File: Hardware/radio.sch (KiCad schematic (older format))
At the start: 8 parts

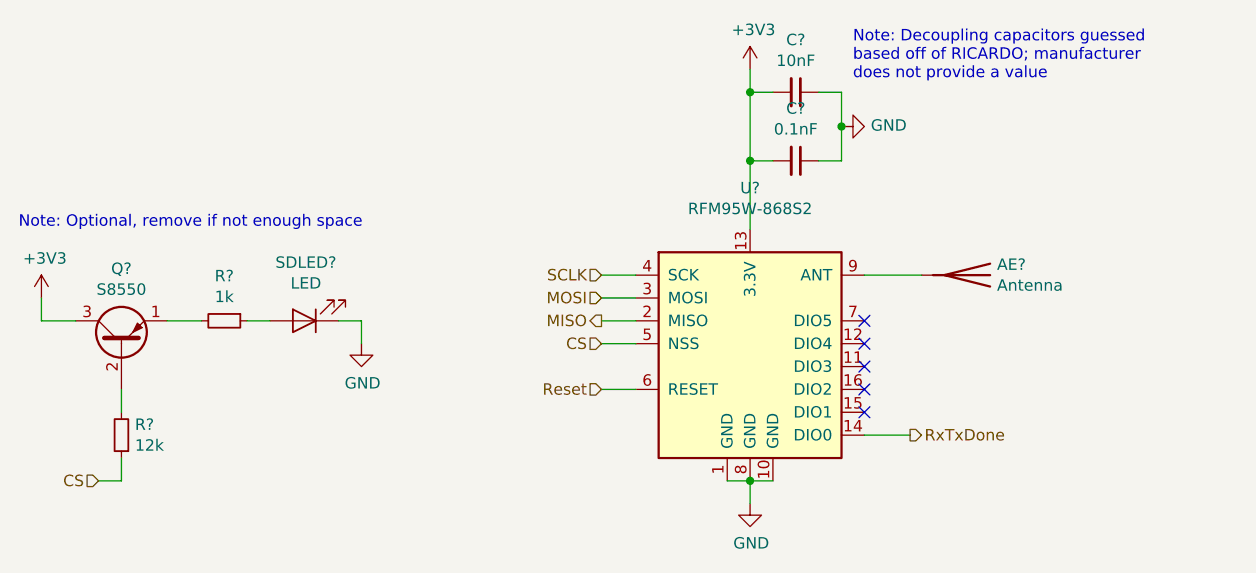
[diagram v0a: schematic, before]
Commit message: Fixed some of the ERC errors
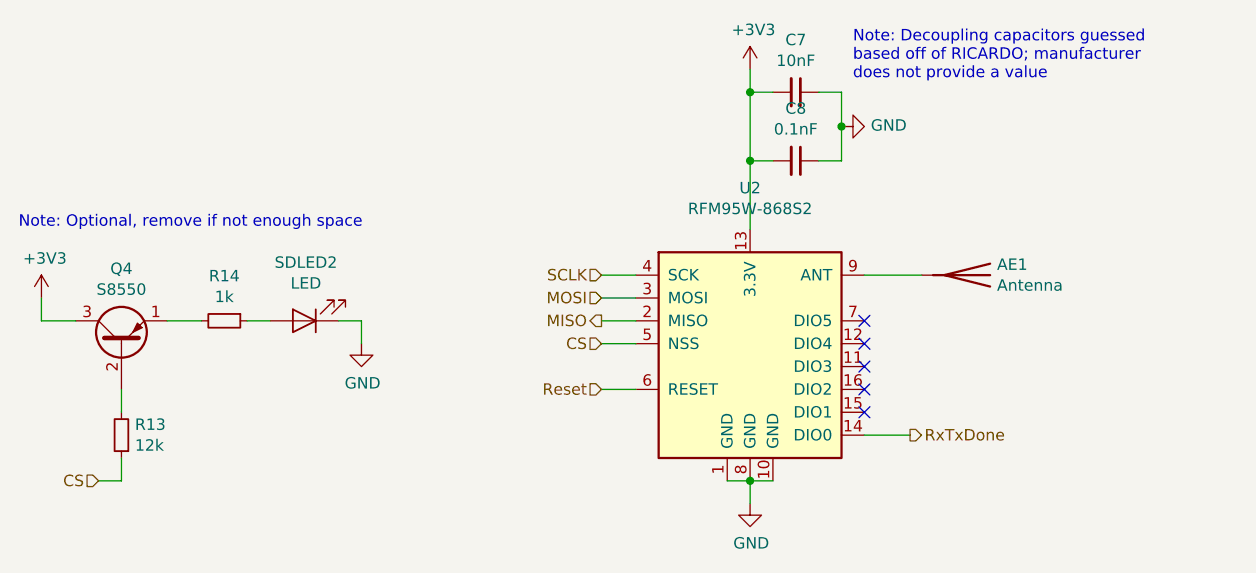
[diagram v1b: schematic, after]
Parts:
- gave numbers to parts that had none: 8
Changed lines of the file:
@@
 $EndDescr
 $Comp
-L RF_Module:RFM95W-868S2 U?
+L RF_Module:RFM95W-868S2 U2
 U 1 1 606C3788
 P 6550 3750
-F 0 "U?" H 6550 4431 50  0000 C CNN
+F 0 "U2" H 6550 4431 50  0000 C CNN
 F 1 "RFM95W-868S2" H 6550 4340 50  0000 C CNN
 F 2 "" H 3250 5400 50  0001 C CNN
@@
 	6550 4350 6550 4450
 $Comp
-L power:GND #PWR0106
+L power:GND #PWR024
 U 1 1 606C4DD1
 P 6550 4450
-F 0 "#PWR0106" H 6550 4200 50  0001 C CNN
+F 0 "#PWR024" H 6550 4200 50  0001 C CNN
 F 1 "GND" H 6555 4277 50  0000 C CNN
 F 2 "" H 6550 4450 50  0001 C CNN
@@
 Connection ~ 6550 2950
 $Comp
-L Device:C_Small C?
+L Device:C_Small C8
 U 1 1 606D342D
 P 6750 2950
-F 0 "C?" V 6521 2950 50  0000 C CNN
+F 0 "C8" V 6521 2950 50  0000 C CNN
 F 1 "0.1nF" V 6612 2950 50  0000 C CNN
 F 2 "" H 6750 2950 50  0001 C CNN
@@
 $EndComp
 $Comp
-L power:+3V3 #PWR0108
+L power:+3V3 #PWR023
 U 1 1 606D3D70
 P 6550 2550
-F 0 "#PWR0108" H 6550 2400 50  0001 C CNN
+F 0 "#PWR023" H 6550 2400 50  0001 C CNN
 F 1 "+3V3" H 6565 2723 50  0000 C CNN
 F 2 "" H 6550 2550 50  0001 C CNN
@@
 	6550 2650 6550 2950
 $Comp
-L Device:C_Small C?
+L Device:C_Small C7
 U 1 1 606DCDA4
 P 6750 2650
-F 0 "C?" V 6521 2650 50  0000 C CNN
+F 0 "C7" V 6521 2650 50  0000 C CNN
 F 1 "10nF" V 6612 2650 50  0000 C CNN
 F 2 "" H 6750 2650 50  0001 C CNN
@@
 $EndComp
 $Comp
-L power:GND #PWR0109
+L power:GND #PWR025
 U 1 1 606DD712
 P 6950 2800
-F 0 "#PWR0109" H 6950 2550 50  0001 C CNN
+F 0 "#PWR025" H 6950 2550 50  0001 C CNN
 F 1 "GND" V 6955 2672 50  0000 R CNN
 F 2 "" H 6950 2800 50  0001 C CNN
@@
 	7050 3450 7300 3450
 $Comp
-L Device:Antenna AE?
+L Device:Antenna AE1
 U 1 1 606E40D7
 P 7500 3450
-F 0 "AE?" V 7454 3580 50  0000 L CNN
+F 0 "AE1" V 7454 3580 50  0000 L CNN
 F 1 "Antenna" V 7545 3580 50  0000 L CNN
 F 2 "" H 7500 3450 50  0001 C CNN
@@
 P 4600 3650
 AR Path="/6068D50F/60A90342" Ref="SDLED?"  Part="1"
-AR Path="/606B714B/60A90342" Ref="RadioLED?"  Part="1"
-F 0 "RadioLED?" H 4593 3395 50  0000 C CNN
+AR Path="/606B714B/60A90342" Ref="SDLED2"  Part="1"
+F 0 "SDLED2" H 4593 3395 50  0000 C CNN
 F 1 "LED" H 4593 3486 50  0000 C CNN
 F 2 "" H 4600 3650 50  0001 C CNN
@@
 	3450 3650 3450 3550
 $Comp
-L power:+3V3 #PWR?
+L power:+3V3 #PWR021
 U 1 1 60A9034C
 P 3450 3550
-F 0 "#PWR?" H 3450 3400 50  0001 C CNN
+F 0 "#PWR021" H 3450 3400 50  0001 C CNN
 F 1 "+3V3" H 3465 3723 50  0000 C CNN
 F 2 "" H 3450 3550 50  0001 C CNN
@@
 $EndComp
 $Comp
-L Device:R_Small R?
+L Device:R_Small R14
 U 1 1 60A90352
 P 4250 3650
-F 0 "R?" V 4054 3650 50  0000 C CNN
+F 0 "R14" V 4054 3650 50  0000 C CNN
 F 1 "1k" V 4145 3650 50  0000 C CNN
 F 2 "" H 4250 3650 50  0001 C CNN
@@
 	4850 3650 4850 3750
 $Comp
-L power:GND #PWR?
+L power:GND #PWR022
 U 1 1 60A9035B
 P 4850 3750
-F 0 "#PWR?" H 4850 3500 50  0001 C CNN
+F 0 "#PWR022" H 4850 3500 50  0001 C CNN
 F 1 "GND" H 4855 3577 50  0000 C CNN
 F 2 "" H 4850 3750 50  0001 C CNN
@@
 P 3800 4150
 AR Path="/6068D50F/60A90361" Ref="R?"  Part="1"
-AR Path="/606B714B/60A90361" Ref="R?"  Part="1"
-F 0 "R?" H 3741 4104 50  0000 R CNN
+AR Path="/606B714B/60A90361" Ref="R13"  Part="1"
+F 0 "R13" H 3741 4104 50  0000 R CNN
 F 1 "12k" H 3741 4195 50  0000 R CNN
 F 2 "" H 3800 4150 50  0001 C CNN
@@
 Note: Optional, remove if not enough space
 $Comp
-L Transistor_BJT:S8550 Q?
+L Transistor_BJT:S8550 Q4
 U 1 1 60A9596C
 P 3800 3750
-F 0 "Q?" V 4128 3750 50  0000 C CNN
+F 0 "Q4" V 4128 3750 50  0000 C CNN
 F 1 "S8550" V 4037 3750 50  0000 C CNN
 F 2 "Package_TO_SOT_THT:TO-92_Inline" H 4000 3675 50  0001 L CIN

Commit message: Created PCB file and laid out components
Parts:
- AE1: footprint (none) -> Connector_PinHeader_2.54mm:PinHeader_1x01_P2.54mm_Vertical
- C7, C8: footprint (none) -> Capacitor_SMD:C_0603_1608Metric
- R13, R14: footprint (none) -> Resistor_SMD:R_0603_1608Metric
- SDLED2: footprint (none) -> LED_SMD:LED_0603_1608Metric
- U2: footprint (none) -> RF_Module:HOPERF_RFM9XW_SMD
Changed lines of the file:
@@
 F 0 "U2" H 6550 4431 50  0000 C CNN
 F 1 "RFM95W-868S2" H 6550 4340 50  0000 C CNN
-F 2 "" H 3250 5400 50  0001 C CNN
+F 2 "RF_Module:HOPERF_RFM9XW_SMD" H 3250 5400 50  0001 C CNN
 F 3 "https://www.hoperf.com/data/upload/portal/20181127/5bfcbea20e9ef.pdf" H 3250 5400 50  0001 C CNN
 	1    6550 3750
@@
 F 0 "C8" V 6521 2950 50  0000 C CNN
 F 1 "0.1nF" V 6612 2950 50  0000 C CNN
-F 2 "" H 6750 2950 50  0001 C CNN
+F 2 "Capacitor_SMD:C_0603_1608Metric" H 6750 2950 50  0001 C CNN
 F 3 "~" H 6750 2950 50  0001 C CNN
 	1    6750 2950
@@
 F 0 "C7" V 6521 2650 50  0000 C CNN
 F 1 "10nF" V 6612 2650 50  0000 C CNN
-F 2 "" H 6750 2650 50  0001 C CNN
+F 2 "Capacitor_SMD:C_0603_1608Metric" H 6750 2650 50  0001 C CNN
 F 3 "~" H 6750 2650 50  0001 C CNN
 	1    6750 2650
@@
 F 0 "AE1" V 7454 3580 50  0000 L CNN
 F 1 "Antenna" V 7545 3580 50  0000 L CNN
-F 2 "" H 7500 3450 50  0001 C CNN
+F 2 "Connector_PinHeader_2.54mm:PinHeader_1x01_P2.54mm_Vertical" H 7500 3450 50  0001 C CNN
 F 3 "~" H 7500 3450 50  0001 C CNN
 	1    7500 3450
@@
 F 0 "SDLED2" H 4593 3395 50  0000 C CNN
 F 1 "LED" H 4593 3486 50  0000 C CNN
-F 2 "" H 4600 3650 50  0001 C CNN
+F 2 "LED_SMD:LED_0603_1608Metric" H 4600 3650 50  0001 C CNN
 F 3 "~" H 4600 3650 50  0001 C CNN
 	1    4600 3650
@@
 F 0 "R14" V 4054 3650 50  0000 C CNN
 F 1 "1k" V 4145 3650 50  0000 C CNN
-F 2 "" H 4250 3650 50  0001 C CNN
+F 2 "Resistor_SMD:R_0603_1608Metric" H 4250 3650 50  0001 C CNN
 F 3 "~" H 4250 3650 50  0001 C CNN
 	1    4250 3650
@@
 F 0 "R13" H 3741 4104 50  0000 R CNN
 F 1 "12k" H 3741 4195 50  0000 R CNN
-F 2 "" H 3800 4150 50  0001 C CNN
+F 2 "Resistor_SMD:R_0603_1608Metric" H 3800 4150 50  0001 C CNN
 F 3 "~" H 3800 4150 50  0001 C CNN
 	1    3800 4150

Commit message: Genuine Confusion
Changed to an ideal diode whatever tf that is
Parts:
- AE1: footprint Connector_PinHeader_2.54mm:PinHeader_1x01_P2.54mm_Vertical -> footprints:max1771cpa&plus_
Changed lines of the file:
@@
 EESchema Schematic File Version 4
+LIBS:VLAD-cache
 EELAYER 30 0
 EELAYER END
@@
 F 0 "AE1" V 7454 3580 50  0000 L CNN
 F 1 "Antenna" V 7545 3580 50  0000 L CNN
-F 2 "Connector_PinHeader_2.54mm:PinHeader_1x01_P2.54mm_Vertical" H 7500 3450 50  0001 C CNN
+F 2 "footprints:max1771cpa&plus_" H 7500 3450 50  0001 C CNN
 F 3 "~" H 7500 3450 50  0001 C CNN
 	1    7500 3450

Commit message: Put EVERYTHING in the 90x90 space
Ofc need to sort out the rats nest better. Nearly there
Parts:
- AE1: footprint footprints:max1771cpa&plus_ -> Connector_Pin:Pin_D1.1mm_L8.5mm_W2.5mm_FlatFork
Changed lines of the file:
@@
 F 0 "AE1" V 7454 3580 50  0000 L CNN
 F 1 "Antenna" V 7545 3580 50  0000 L CNN
-F 2 "footprints:max1771cpa&plus_" H 7500 3450 50  0001 C CNN
+F 2 "Connector_Pin:Pin_D1.1mm_L8.5mm_W2.5mm_FlatFork" H 7500 3450 50  0001 C CNN
 F 3 "~" H 7500 3450 50  0001 C CNN
 	1    7500 3450
